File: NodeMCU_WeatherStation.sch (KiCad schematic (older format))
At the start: 24 parts, among them J12 Screw_Terminal_01x02, J14 Screw_Terminal_01x02, J15 Conn_01x10, J4 Conn_01x04, J5 Conn_01x04, U1 BME280, U7 R-785.0-0.5

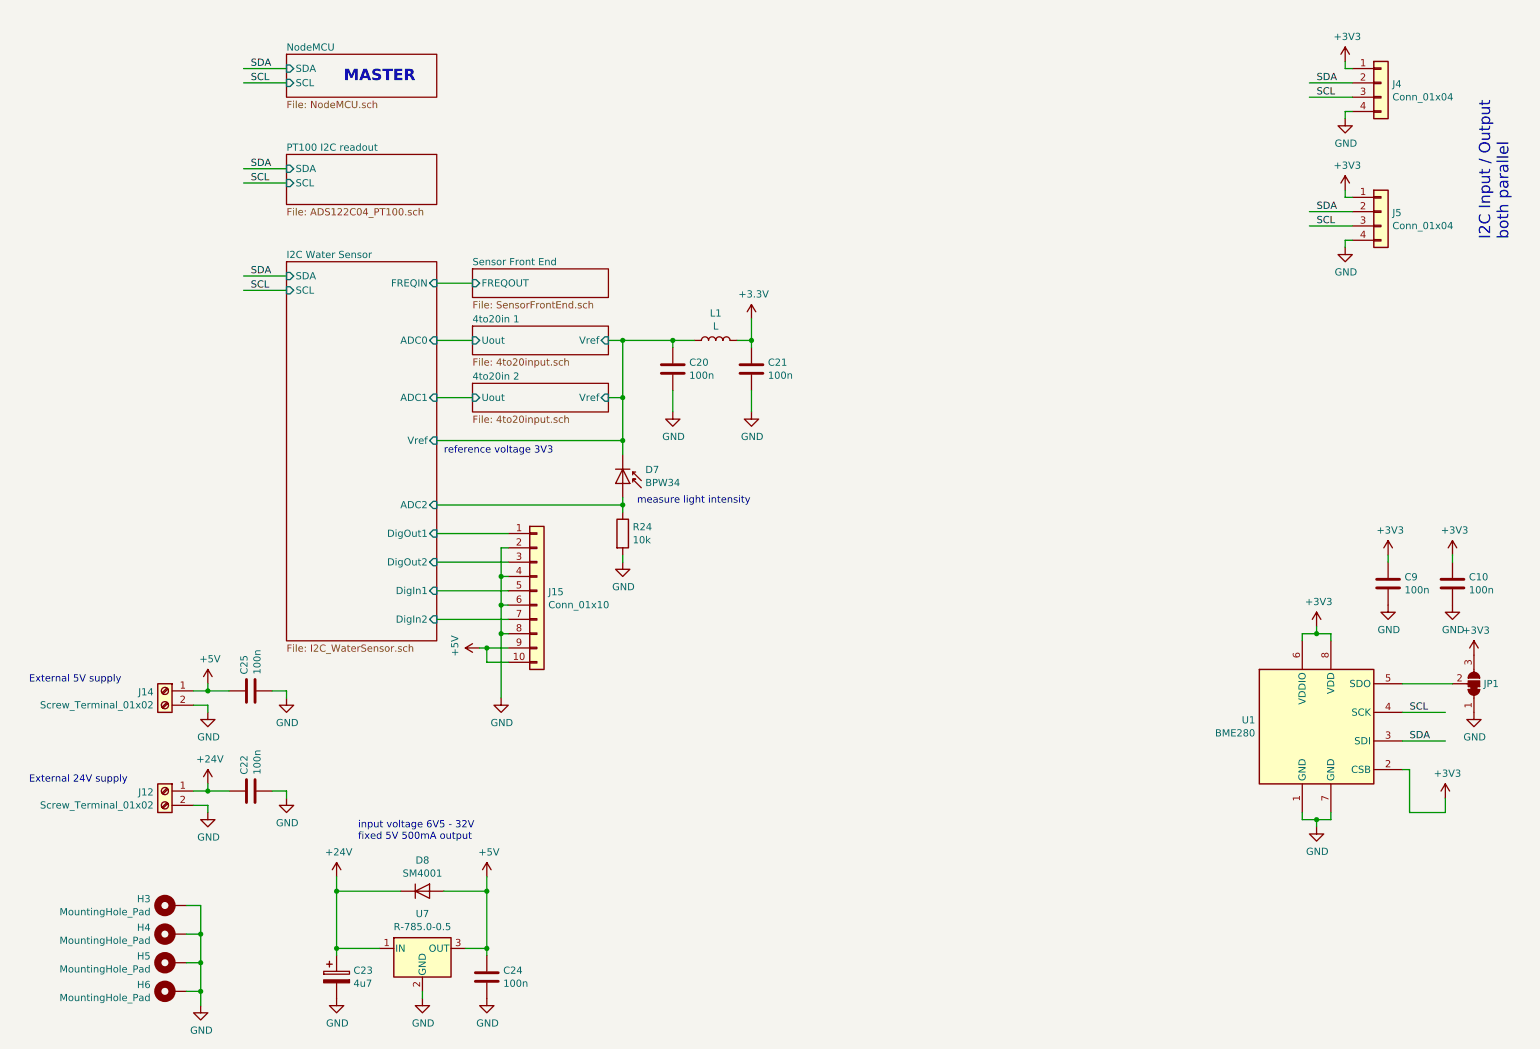
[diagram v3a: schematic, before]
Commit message: changed to 3.2mm holes for mounting the PCB
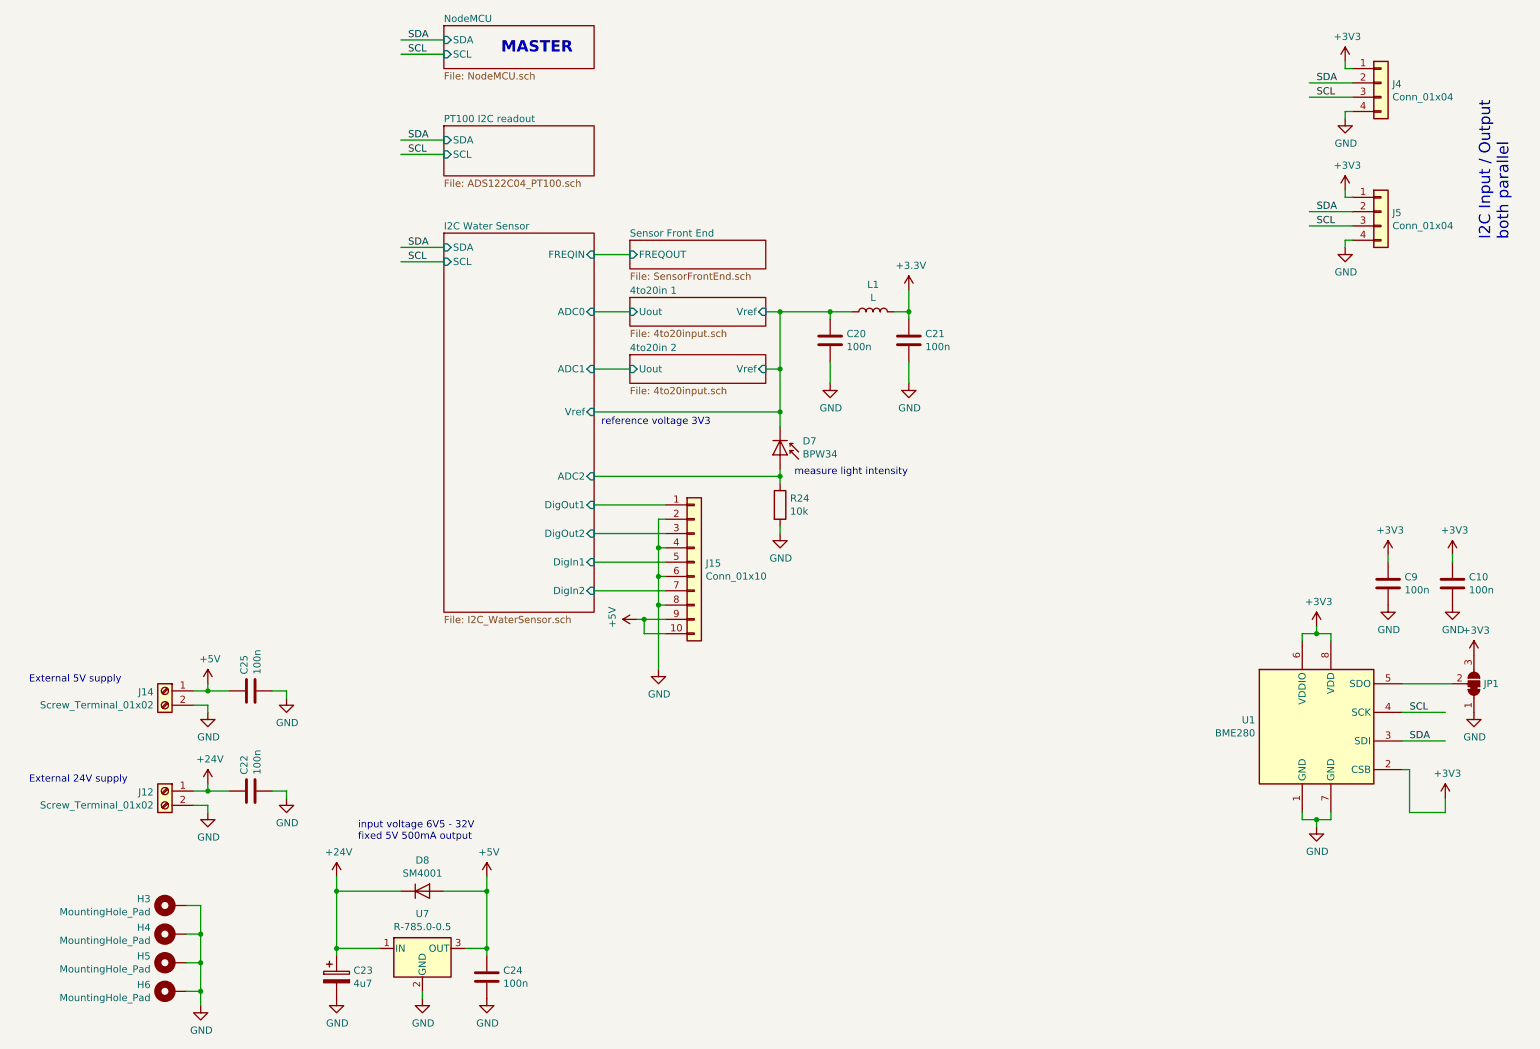
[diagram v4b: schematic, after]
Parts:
- H3, H4, H5, H6: footprint MountingHole:MountingHole_4.3mm_M4_Pad_Via -> MountingHole:MountingHole_3.2mm_M3_Pad_Via
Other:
- moved on the sheet: C20, C21, D7, J15, L1, R24

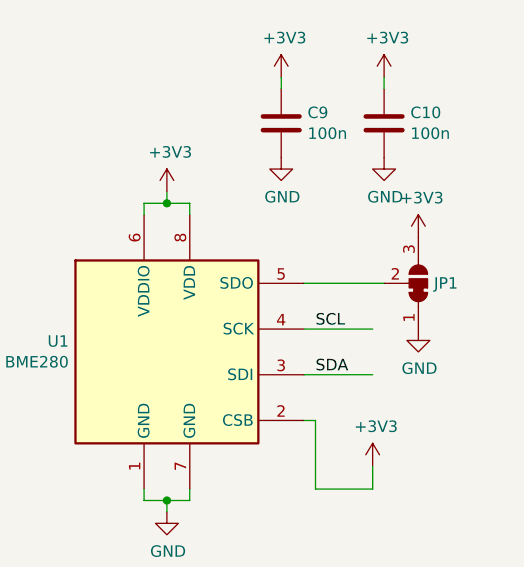
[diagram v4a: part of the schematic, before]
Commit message: included address jumper for AVR, which makes it easier to use multiple of these boards at the same I2C bus.
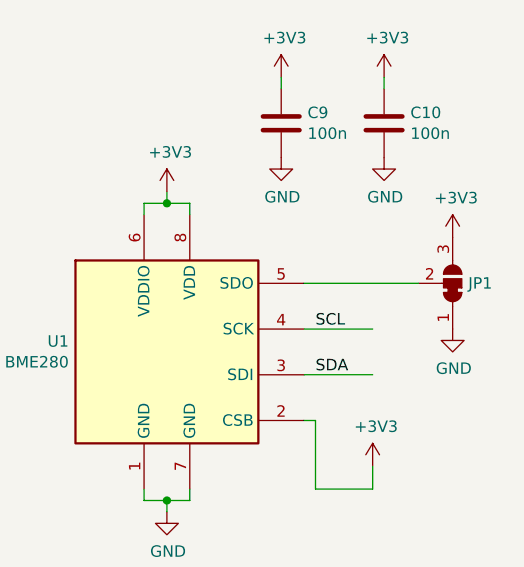
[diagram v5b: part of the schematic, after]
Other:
- moved on the sheet: JP1
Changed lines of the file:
@@
 Text Label 10200 5450 0    50   ~ 0
 SCL
-Wire Wire Line
-	10150 5250 10500 5250
 $Comp
 L power:+3V3 #PWR?
 U 1 1 5ECCCCFF
-P 10650 5050
+P 10800 5050
 AR Path="/5E788D14/5ECCCCFF" Ref="#PWR?"  Part="1"
 AR Path="/5ECCCCFF" Ref="#PWR035"  Part="1"
-F 0 "#PWR035" H 10650 4900 50  0001 C CNN
-F 1 "+3V3" H 10665 5223 50  0000 C CNN
-F 2 "" H 10650 5050 50  0001 C CNN
-F 3 "" H 10650 5050 50  0001 C CNN
-	1    10650 5050
+F 0 "#PWR035" H 10800 4900 50  0001 C CNN
+F 1 "+3V3" H 10815 5223 50  0000 C CNN
+F 2 "" H 10800 5050 50  0001 C CNN
+F 3 "" H 10800 5050 50  0001 C CNN
+	1    10800 5050
 	1    0    0    -1
 $EndComp
@@
 L power:GND #PWR?
 U 1 1 5ECCC4C4
-P 10650 5450
+P 10800 5450
 AR Path="/5E788D14/5ECCC4C4" Ref="#PWR?"  Part="1"
 AR Path="/5ECCC4C4" Ref="#PWR036"  Part="1"
-F 0 "#PWR036" H 10650 5200 50  0001 C CNN
-F 1 "GND" H 10655 5277 50  0000 C CNN
-F 2 "" H 10650 5450 50  0001 C CNN
-F 3 "" H 10650 5450 50  0001 C CNN
-	1    10650 5450
+F 0 "#PWR036" H 10800 5200 50  0001 C CNN
+F 1 "GND" H 10805 5277 50  0000 C CNN
+F 2 "" H 10800 5450 50  0001 C CNN
+F 3 "" H 10800 5450 50  0001 C CNN
+	1    10800 5450
 	1    0    0    -1
 $EndComp
@@
 L Jumper:SolderJumper_3_Bridged12 JP1
 U 1 1 5ECCA3BC
-P 10650 5250
-F 0 "JP1" V 10650 5318 50  0000 L CNN
-F 1 "SolderJumper_3_Bridged12" V 10605 5318 50  0001 L CNN
-F 2 "Jumper:SolderJumper-3_P1.3mm_Bridged12_Pad1.0x1.5mm" H 10650 5250 50  0001 C CNN
-F 3 "~" H 10650 5250 50  0001 C CNN
-	1    10650 5250
+P 10800 5250
+F 0 "JP1" V 10800 5318 50  0000 L CNN
+F 1 "SolderJumper_3_Bridged12" V 10755 5318 50  0001 L CNN
+F 2 "Jumper:SolderJumper-3_P1.3mm_Bridged12_Pad1.0x1.5mm" H 10800 5250 50  0001 C CNN
+F 3 "~" H 10800 5250 50  0001 C CNN
+	1    10800 5250
 	0    1    -1   0
 $EndComp
@@
 	4850 4800 4800 4800
 Connection ~ 4850 4800
+Wire Wire Line
+	10150 5250 10650 5250
 $EndSCHEMATC

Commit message: include latest changes
latest changes to design
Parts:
- added J16: Conn_01x02, Connector_PinHeader_2.54mm:PinHeader_1x02_P2.54mm_Vertical, symbol Connector_Generic:Conn_01x02
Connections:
- wire segments 107 -> 110
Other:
- note added: "Housing RND 455-00208"
- moved on the sheet: C20, C21, D7, J15, L1, R24
